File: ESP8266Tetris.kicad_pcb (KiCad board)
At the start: 2 copper layers, 69 x 132 mm, 213 parts, among them J1 10118192-0001LF, Q1 BC847BLT1G, Q2 DMP3068L-7, Q3 BC847BLT1G, Q4 BC847BLT1G, Q5 BC847BLT1G, SW1 B3AL-1006P, SW2 B3AL-1006P, SW3 B3AL-1006P, SW4 B3AL-1006P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

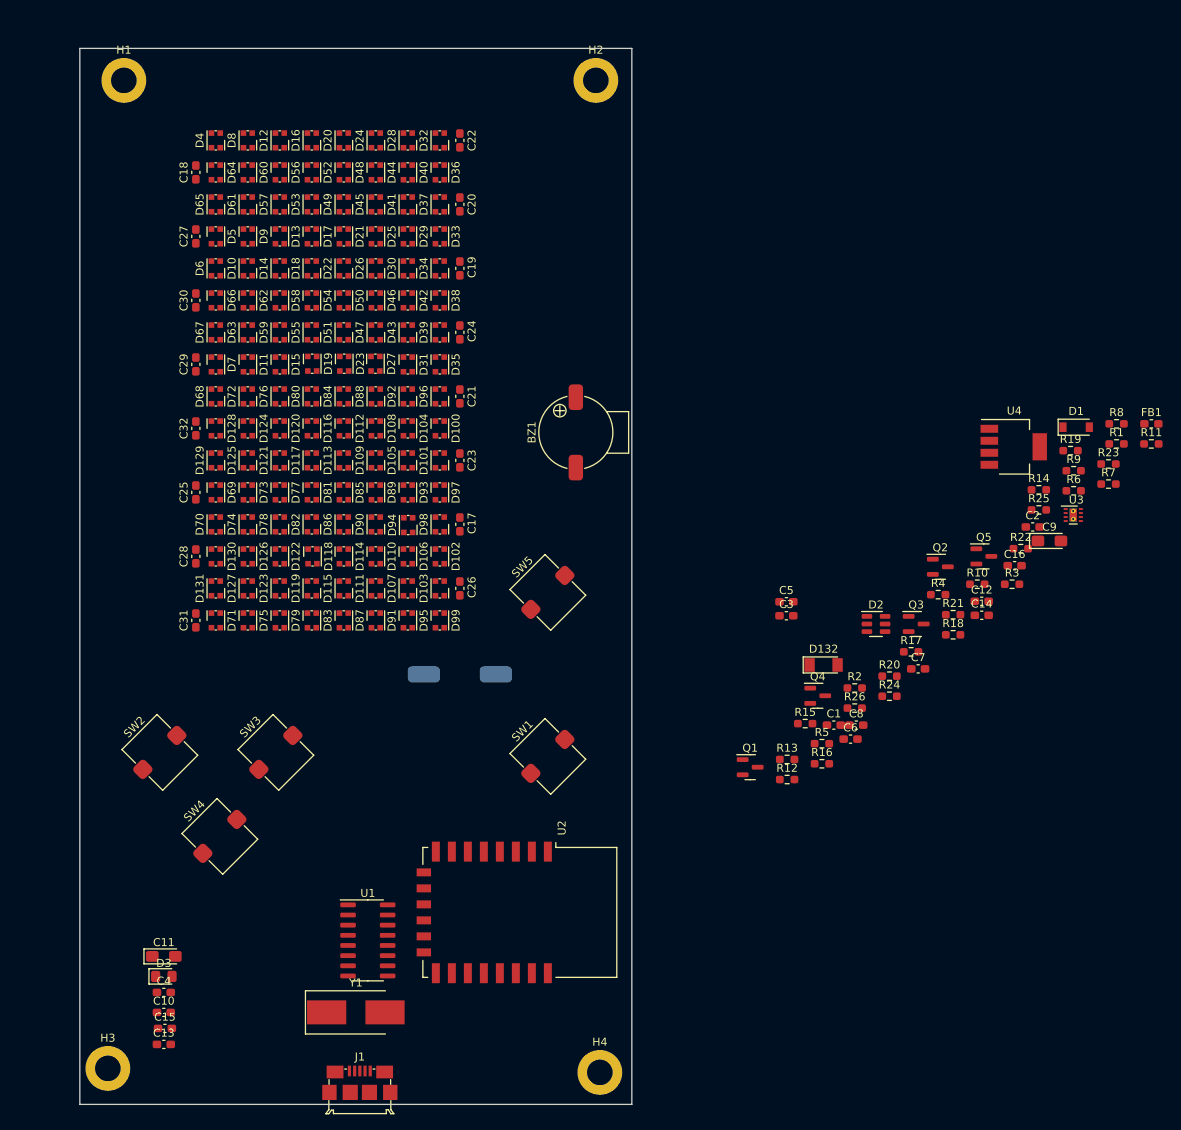
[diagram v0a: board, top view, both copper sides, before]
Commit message: Schematic finished, routing PCB started.
Signed-off-by: Ion Bold <bold.ion86@gmail.com>
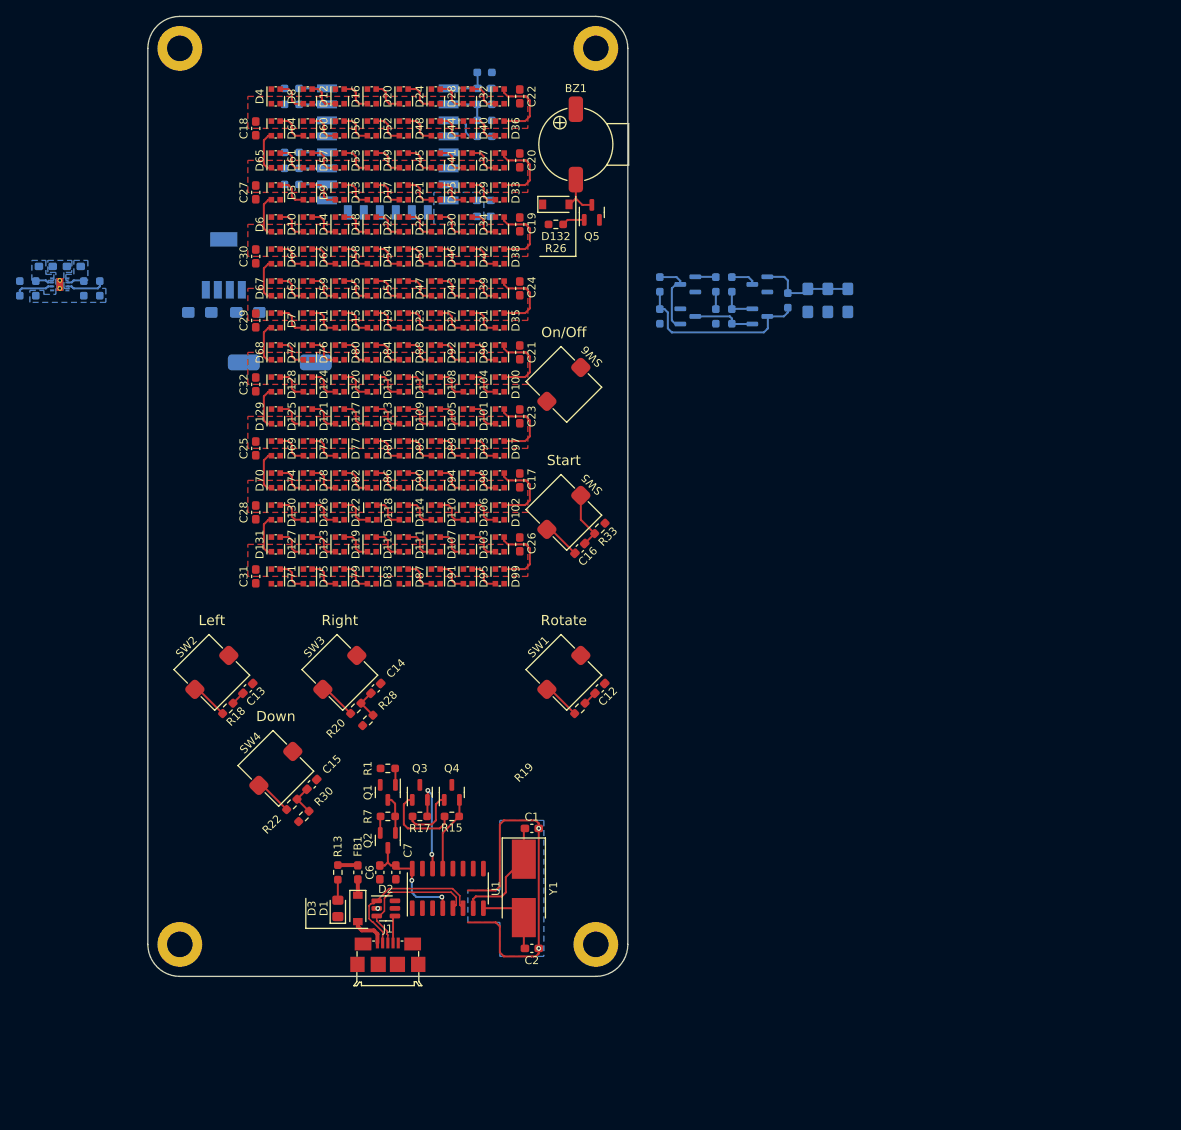
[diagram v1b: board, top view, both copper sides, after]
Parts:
- removed R24: 100R, Resistor_SMD:R_0603_1608Metric_Pad0.98x0.95mm_HandSolder
- added C33: TAJA106K016RNJ, Capacitor_Tantalum_SMD:CP_EIA-3216-12_Kemet-S_Pad1.58x1.35mm_HandSolder, B.Cu at (187.5, 65.5)
- added C34: TAJA106K016RNJ, Capacitor_Tantalum_SMD:CP_EIA-3216-12_Kemet-S_Pad1.58x1.35mm_HandSolder, B.Cu at (182.5, 65.5)
- added C35: TAJA106K016RNJ, Capacitor_Tantalum_SMD:CP_EIA-3216-12_Kemet-S_Pad1.58x1.35mm_HandSolder, B.Cu at (185.0, 65.5)
- added Q6: DMP3068L-7, Package_TO_SOT_SMD:SOT-23, B.Cu at (176.5, 67.5)
- added Q7: BC847BLT1G, Package_TO_SOT_SMD:SOT-23, B.Cu at (167.5, 67.5)
- added Q8: BC847BLT1G, Package_TO_SOT_SMD:SOT-23, B.Cu at (167.5, 63.5)
- added Q9: BC847BLT1G, Package_TO_SOT_SMD:SOT-23, B.Cu at (176.5, 63.5)
- added R27: 100k, Resistor_SMD:R_0603_1608Metric_Pad0.98x0.95mm_HandSolder, B.Cu at (173.0, 63.5)
- added R28: 10k, Resistor_SMD:R_0603_1608Metric_Pad0.98x0.95mm_HandSolder, F.Cu at (127.5, 118.0)
- added R29: 1M, Resistor_SMD:R_0603_1608Metric_Pad0.98x0.95mm_HandSolder, B.Cu at (180.0, 65.5)
- added R30: 10k, Resistor_SMD:R_0603_1608Metric_Pad0.98x0.95mm_HandSolder, F.Cu at (119.5, 130.0)
- added R31: 3k3, Resistor_SMD:R_0603_1608Metric_Pad0.98x0.95mm_HandSolder, B.Cu at (142.1, 43.0)
- added R32: 1k, Resistor_SMD:R_0603_1608Metric_Pad0.98x0.95mm_HandSolder, B.Cu at (142.1, 41.0)
- added R33: 100R, Resistor_SMD:R_0603_1608Metric_Pad0.98x0.95mm_HandSolder, F.Cu at (156.5, 94.0)
- added R34: 10k, Resistor_SMD:R_0603_1608Metric_Pad0.98x0.95mm_HandSolder, B.Cu at (164.0, 67.5)
- added SW6: B3AL-1006P, KiCadCustom:SW_SPST_Omron_B3AL-100xP, F.Cu at (152.0, 76.0)
- C10, C11, C3, C4, C5, C8, C9, R10, R11, R12, R14, R2, R23, R25, R3, R4, R5, R6, R8, R9, U2, U4: moved to B.Cu
- C12, C13, C14, C15, C16: value 100n -> 10n
- D132: value D_Small -> 1N4148W-7-F; footprint Diode_SMD:D_MiniMELF -> Diode_SMD:D_SOD-123
- R16: value 100R -> 100k; moved to B.Cu
- R19: value 10k -> 100R
- R21: value 10k -> 100k; moved to B.Cu
- R26: value 220R -> 470R
- U3: value BQ25170 -> BQ25170DSGR; moved to B.Cu
- moved R11 140.8 mm to (86.0, 64.0), turned to -90 degrees
- moved R8 130.2 mm to (92.0, 64.0), turned to -90 degrees
- moved U3 129.9 mm to (89.0, 63.5), turned to 180 degrees
- moved R14 129.8 mm to (84.0, 64.0), turned to 90 degrees
- moved FB1 113.9 mm to (126.2, 137.0), turned to 90 degrees
- moved D1 108.1 mm to (126.2, 141.5), turned to -90 degrees
- moved R9 107.9 mm to (118.0, 41.0)
- moved R10 105.7 mm to (118.0, 39.0)
- moved R12 105.6 mm to (94.0, 64.0), turned to -90 degrees
- moved R6 105.0 mm to (118.0, 51.0)
- moved C9 104.2 mm to (112.5, 67.0)
- moved U4 101.3 mm to (109.5, 61.1), turned to 90 degrees
- moved U2 100.9 mm to (130.0, 42.5), turned to 180 degrees
- moved R1 99.7 mm to (130.0, 124.0), turned to 180 degrees
- moved R7 99.2 mm to (130.0, 130.0)
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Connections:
- C12 pad 1: +3V3 -> ROTATE
- C12 pad 2: ROTATE -> GND
- C13 pad 1: +3V3 -> LEFT
- C13 pad 2: Net-(C13-Pad2) -> GND
- C14 pad 1: +3V3 -> RIGHT
- C14 pad 2: Net-(C14-Pad2) -> GND
- C15 pad 1: +3V3 -> DOWN
- C15 pad 2: Net-(C15-Pad2) -> GND
- C16 pad 2: Net-(C16-Pad2) -> Net-(R33-Pad2)
- D2 pad 1: unconnected-(D2-Pad1) -> USB_D_N
- D2 pad 3: USB_D_N -> USB_D_P
- D2 pad 4: USB_D_P -> Net-(D2-Pad4)
- D2 pad 6: Net-(D2-Pad6) -> unconnected-(D2-Pad6)
- D3 pad 2: +5V -> Net-(D3-Pad2)
- J1 pad 4: Net-(D2-Pad6) -> Net-(D2-Pad4)
- Q4 pad 3: GPIO0 -> LEFT
- R13 pad 1: Net-(R13-Pad1) -> Net-(D3-Pad2)
- R13 pad 2: Net-(D3-Pad1) -> +5V
- R16 pad 1: Net-(R16-Pad1) -> Net-(Q6-Pad1)
- R16 pad 2: ROTATE -> BAT
- R18 pad 2: Net-(C13-Pad2) -> Net-(R18-Pad2)
- R19 pad 1: Net-(C13-Pad2) -> ROTATE
- R19 pad 2: GND -> Net-(R19-Pad2)
- R20 pad 2: Net-(C14-Pad2) -> Net-(R20-Pad2)
- R21 pad 1: Net-(C14-Pad2) -> Net-(Q7-Pad1)
- R21 pad 2: GND -> Net-(Q6-Pad3)
- R22 pad 2: Net-(C15-Pad2) -> Net-(R22-Pad2)
- R23 pad 1: Net-(C15-Pad2) -> Net-(Q8-Pad1)
- R23 pad 2: GND -> SD
- R25 pad 1: Net-(C16-Pad2) -> GND
- R25 pad 2: GND -> SD
- R4 pad 2: GPIO0 -> LEFT
- R5 pad 2: SD -> ROTATE
- R6 pad 2: ROTATE -> START
- SW1 pad 1: +3V3 -> Net-(R19-Pad2)
- SW1 pad 2: ROTATE -> GND
- SW2 pad 1: +3V3 -> Net-(R18-Pad2)
- SW2 pad 2: Net-(C13-Pad2) -> GND
- SW3 pad 1: +3V3 -> Net-(R20-Pad2)
- SW3 pad 2: Net-(C14-Pad2) -> GND
- SW4 pad 1: +3V3 -> Net-(R22-Pad2)
- SW4 pad 2: Net-(C15-Pad2) -> GND
- SW5 pad 2: Net-(C16-Pad2) -> Net-(R33-Pad2)
- U2 pad 16: Net-(R16-Pad1) -> START
- U2 pad 17: SD -> ROTATE
- U2 pad 18: GPIO0 -> LEFT
- U2 pad 20: LEFT -> SD
- U2 pad 4: START -> unconnected-(U2-Pad4)
- U3 pad 5: Net-(R13-Pad1) -> Net-(D3-Pad1)
- U4 pad 1: SD -> ON
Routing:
- net GND: track 0.00 -> 46.1 mm, vias 0 -> 3
- net Net-(Q6-Pad3): track 0.00 -> 23.1 mm
- net USB_D_N: track 0.00 -> 19.8 mm
- net USB_D_P: track 0.00 -> 17.8 mm
- net Net-(C6-Pad1): track 0.00 -> 14.8 mm, vias 0 -> 2
- net Net-(C1-Pad1): track 0.00 -> 14.6 mm
- net RTS: track 0.00 -> 13.3 mm, vias 0 -> 2
- net Net-(C33-Pad1): track 0.00 -> 12.1 mm
- net Net-(Q3-Pad1): track 0.00 -> 10.2 mm
- net Net-(Q7-Pad1): track 0.00 -> 9.72 mm
- net Net-(D103-Pad1): track 0.00 -> 9.51 mm
- net Net-(D100-Pad3): track 0.00 -> 9.51 mm
- net Net-(D34-Pad1): track 0.00 -> 9.51 mm
- net Net-(D33-Pad3): track 0.00 -> 9.51 mm
- net Net-(D32-Pad1): track 0.00 -> 9.51 mm
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- added copper zone on B.Cu, net +3V3
- added copper zone on F.Cu, net +3V3
- added copper zone on B.Cu, net +5V
- added copper zone on B.Cu, net BAT
- added copper zone on B.Cu, net GND
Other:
- board size 69 x 132 mm -> 60 x 120 mm
- board text added: "Down"
- board text added: "Left"
- board text added: "On/Off"
- board text added: "Right"
- board text added: "Rotate"
- board text added: "Start"

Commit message: Routing PCB done.
Signed-off-by: Ion Bold <bold.ion86@gmail.com>
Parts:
- added G***: LOGO, KiCadCustom:IBLogo, F.Cu at (139.2, 112.0)
- Y1: footprint Crystal:Crystal_SMD_7050-2Pin_7.0x5.0mm_HandSoldering -> Crystal:Crystal_SMD_7050-2Pin_7.0x5.0mm
- moved C33 33.0 mm to (154.5, 65.5)
- moved C34 33.0 mm to (149.5, 65.5)
- moved C35 33.0 mm to (152.0, 65.5)
- moved Q6 33.0 mm to (143.5, 67.5)
- moved Q7 33.0 mm to (134.5, 67.5)
- moved Q8 33.0 mm to (134.5, 63.5)
- moved Q9 33.0 mm to (143.5, 63.5)
- moved R16 33.0 mm to (140.0, 67.5)
- moved R21 33.0 mm to (131.0, 63.5)
- moved R23 33.0 mm to (138.0, 63.5)
- moved R25 33.0 mm to (138.0, 67.5)
- moved R27 33.0 mm to (140.0, 63.5)
- moved R29 33.0 mm to (147.0, 65.5)
- moved R34 33.0 mm to (131.0, 67.5)
- moved R14 32.5 mm to (116.5, 62.5), turned to -90 degrees
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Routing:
- net +3V3: track 6.83 -> 191.5 mm, vias 0 -> 18
- net Net-(R10-Pad1): track 0.00 -> 153.0 mm, vias 0 -> 1
- net Net-(R9-Pad1): track 0.00 -> 149.9 mm, vias 0 -> 1
- net DOWN: track 3.88 -> 148.1 mm, vias 0 -> 1
- net ROTATE: track 5.25 -> 136.2 mm, vias 0 -> 1
- net +5V: track 2.52 -> 132.9 mm, vias 0 -> 2
- net RST: track 5.65 -> 131.2 mm, vias 0 -> 1
- net LEFT: track 5.25 -> 127.5 mm, vias 0 -> 1
- net Net-(D3-Pad1): track 0.00 -> 113.9 mm, vias 0 -> 1
- net RIGHT: track 3.88 -> 115.0 mm, vias 0 -> 3
- net START: track 3.49 -> 111.7 mm, vias 0 -> 1
- net SD: track 2.18 -> 70.2 mm, vias 0 -> 2
- net Net-(Q6-Pad3): track 23.1 -> 74.2 mm
- net BUZZER: track 0.00 -> 37.8 mm, vias 0 -> 1
- net Net-(Q7-Pad1): track 9.72 -> 43.6 mm, vias 0 -> 1
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- added copper zone on F.Cu, net GND
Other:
- board text added: "1"
- board text added: "2"
- board text added: "LiPo 3.7V"
- board text added: "v1.0"

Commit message: Fabrication and assembly files generated (v1.0).
Signed-off-by: Ion Bold <bold.ion86@gmail.com>
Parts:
- added G***: LOGO, KiCadCustom:Z_LOGO, B.Cu at (152.0, 48.0)
- added G***: LOGO, KiCadCustom:Z_LOGO, B.Cu at (108.0, 48.0)
- added H5: Hole, MountingHole:MountingHole_2.2mm_M2, F.Cu at (147.5, 104.2)
- added H6: Hole, MountingHole:MountingHole_2.2mm_M2, F.Cu at (112.5, 104.2)
- added H7: Hole, MountingHole:MountingHole_2.2mm_M2, F.Cu at (112.5, 35.8)
- added H8: Hole, MountingHole:MountingHole_2.2mm_M2, F.Cu at (147.5, 35.8)
- C11, C33, C34, C35, C9: footprint Capacitor_Tantalum_SMD:CP_EIA-3216-12_Kemet-S_Pad1.58x1.35mm_HandSolder -> Capacitor_Tantalum_SMD:CP_EIA-3216-18_Kemet-A_Pad1.58x1.35mm_HandSolder
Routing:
- net +3V3: track 191.5 -> 186.1 mm, vias 18 -> 17

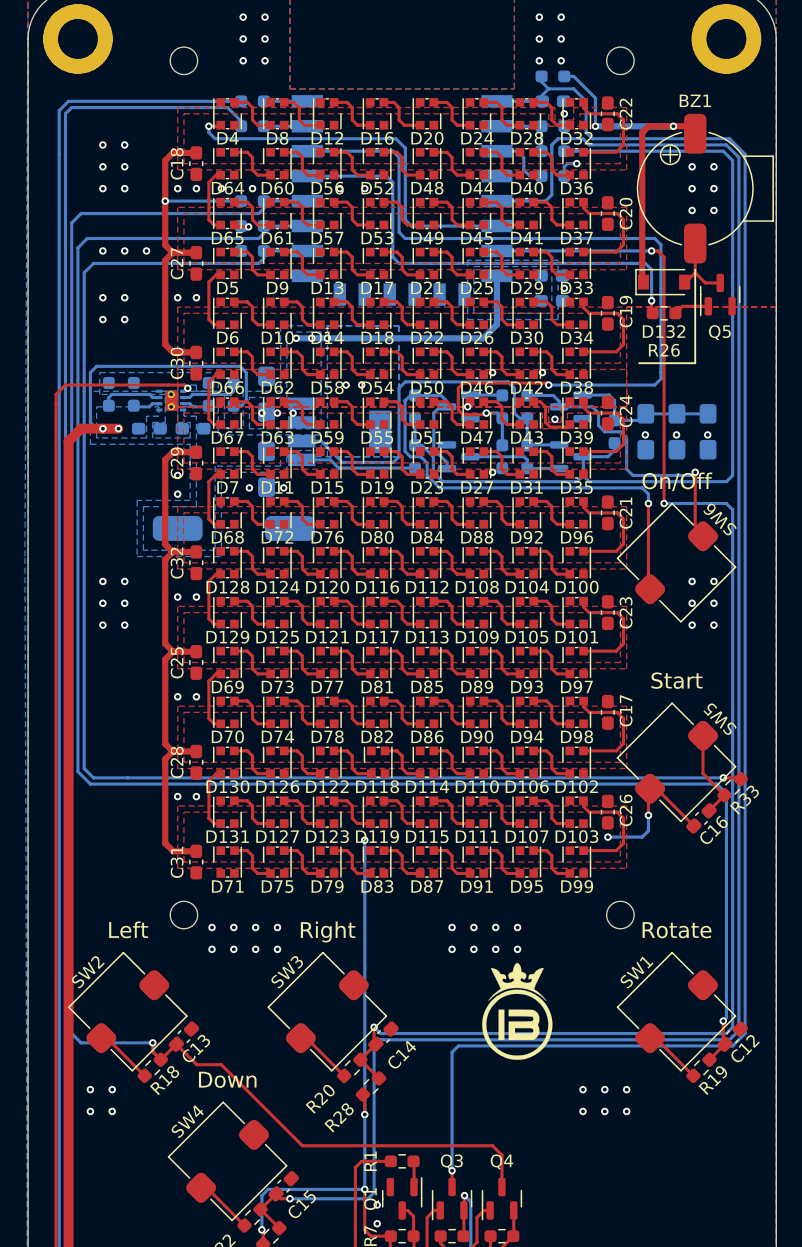
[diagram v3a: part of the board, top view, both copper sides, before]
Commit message: Buzzer moved to bottom layer, fabrication and assembly files regenerated.
Signed-off-by: Ion Bold <bold.ion86@gmail.com>
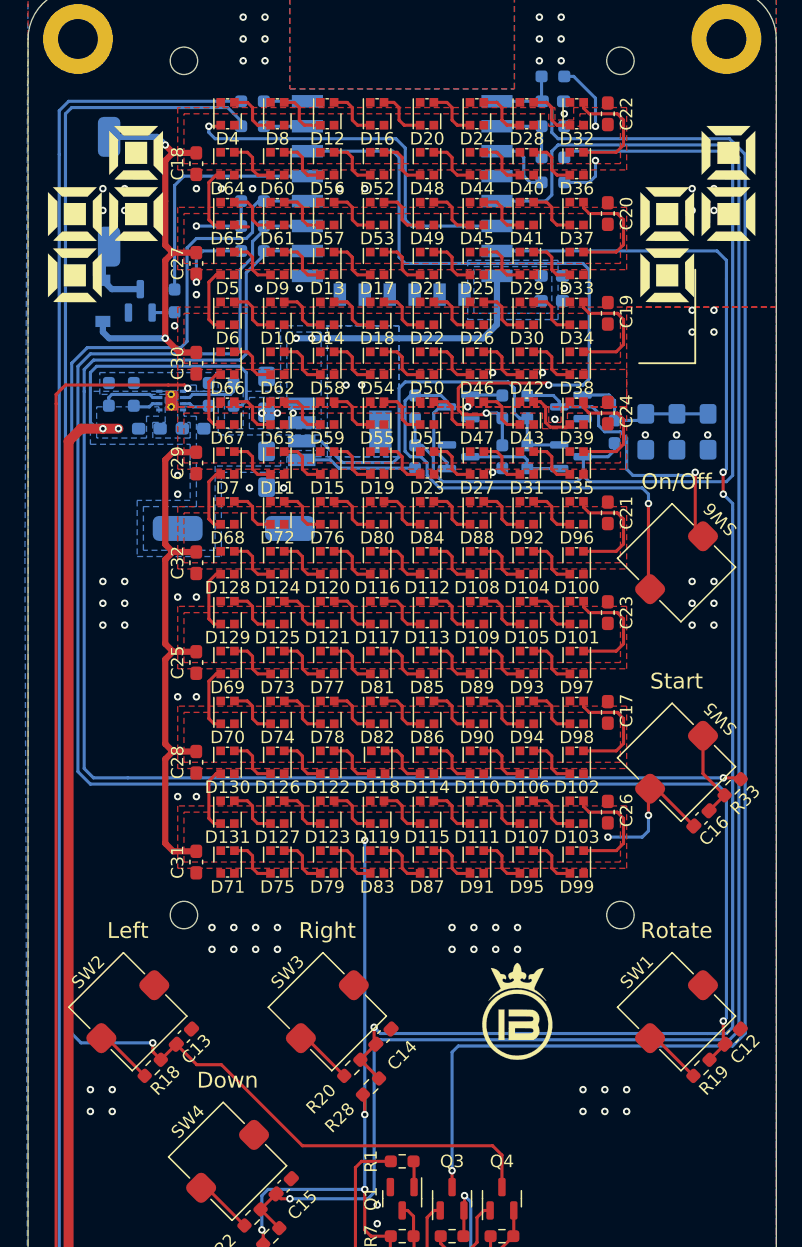
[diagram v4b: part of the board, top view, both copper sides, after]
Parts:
- BZ1, D132, Q5, R26: moved to B.Cu
- G*** (x2): moved to F.Cu
- moved BZ1 47.0 mm to (106.5, 46.2)
- moved Q5 46.5 mm to (109.0, 55.0)
- moved D132 45.0 mm to (106.0, 55.0), turned to 90 degrees
- moved R26 39.3 mm to (111.8, 55.0), turned to -90 degrees
- moved G*** 1.75 mm to (153.8, 48.0)
- moved G*** 1.75 mm to (106.2, 48.0)
- moved R3 0.50 mm to (142.1, 45.5)
- moved R31 0.50 mm to (142.1, 43.5)
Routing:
- net BUZZER: track 37.8 -> 19.3 mm, vias 1 -> 0
- net SD: track 70.2 -> 58.7 mm
- net +3V3: track 186.1 -> 175.5 mm
- net GND: track 56.8 -> 62.6 mm, vias 118 -> 113
- net LEFT: track 127.5 -> 126.1 mm
- net ROTATE: track 136.2 -> 135.1 mm
- net Net-(Q5-Pad1): track 2.87 -> 1.81 mm
- net START: track 111.7 -> 110.8 mm
- net DOWN: track 148.1 -> 147.4 mm
- net RST: track 130.9 -> 130.3 mm
- net BATMS: track 5.58 -> 6.08 mm
